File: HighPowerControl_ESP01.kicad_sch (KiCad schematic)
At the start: 9 parts, among them J1 ESP-01, J2 AC Input, J4 AMS1117Module, J4 To SSR

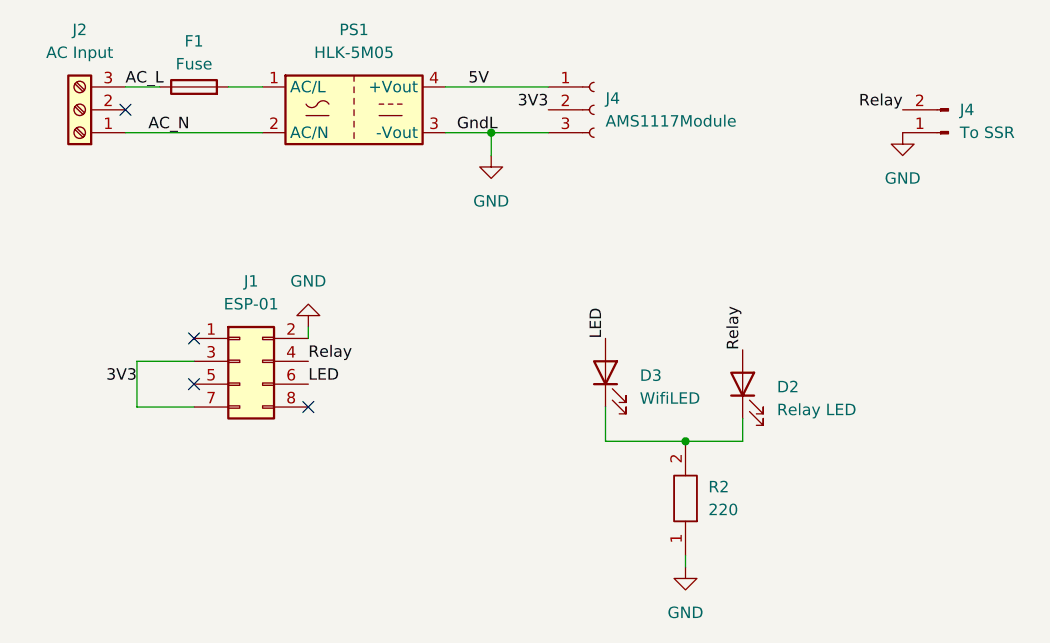
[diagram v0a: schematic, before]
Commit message: Flip the HiLInk AC-DC converter footprint
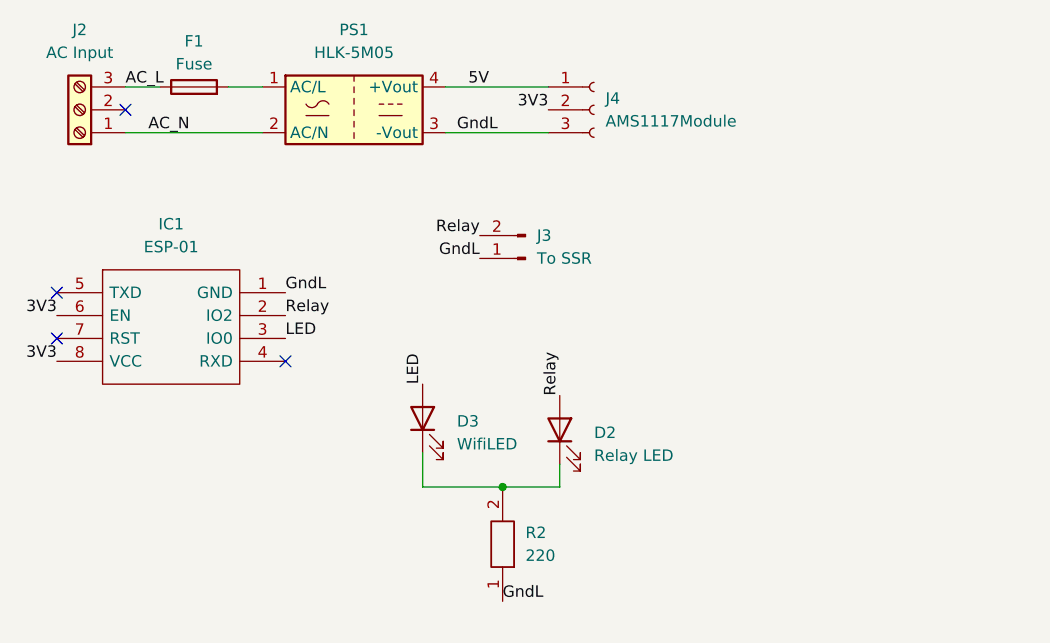
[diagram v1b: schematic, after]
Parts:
- removed J1: ESP-01, Connector_PinSocket_2.54mm:PinSocket_2x04_P2.54mm_Vertical, symbol Connector_Generic:Conn_02x04_Odd_Even
- added IC1: ESP-01, ESP-01:ESP01, symbol ESP:ESP-01
- renumbered J4 to J3
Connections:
- net 3V3: now also IC1.6 (EN), IC1.8 (VCC)
- net LED: now also IC1.3 (IO0)
- net Relay: now also IC1.2 (IO2)
- net GND renamed GndL
- net GndL: now also IC1.1 (GND)
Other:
- moved on the sheet: D2, D3, J3, R2

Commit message: Inverting logic of SSR
when SSR is connected to the GPIO it causes an issue in the boot of ESP-01
So the circuit was changed slightly based on the suggestions  in https://arduino.stackexchange.com/questions/37303/esp8266-esp-01-not-booting-with-load-on-io-pin-2
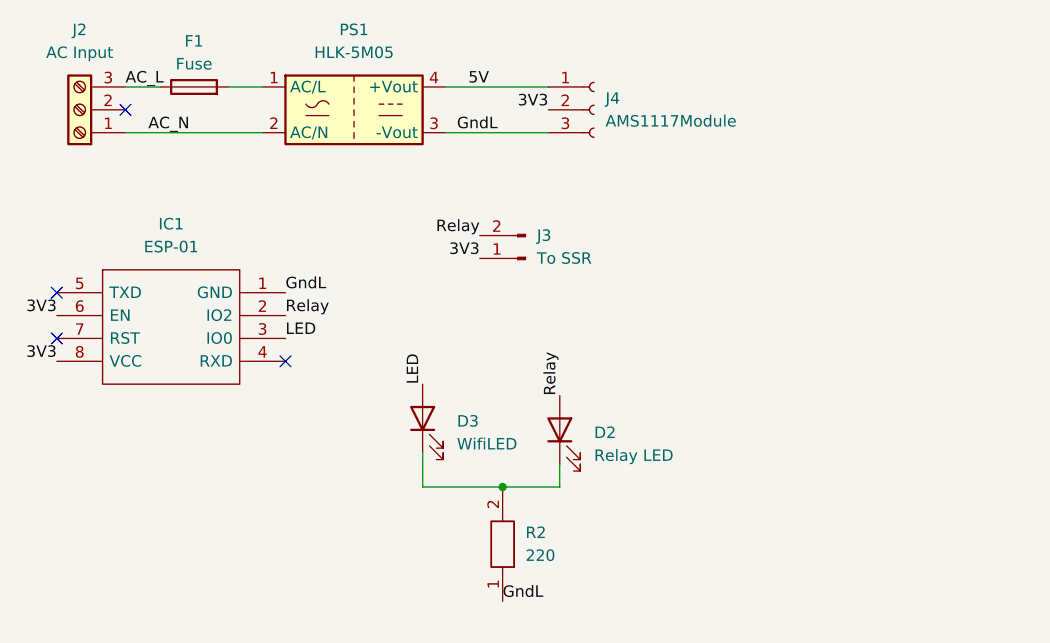
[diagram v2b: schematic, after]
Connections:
- net 3V3: now also J3.1 (Pin_1)
- net GndL: no longer J3.1 (Pin_1)
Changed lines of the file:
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@@
     (effects (font (size 1.27 1.27)) (justify right bottom))
   )
-  (label "GndL" (at 69.85 44.45 180) (fields_autoplaced)
+  (label "3V3" (at 69.85 44.45 180) (fields_autoplaced)
     (effects (font (size 1.27 1.27)) (justify right bottom))
   )
